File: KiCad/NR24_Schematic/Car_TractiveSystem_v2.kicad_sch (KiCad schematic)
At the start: 26 parts, among them J1 M_con, J2 F_con, J5 Dash TI Connection, J6 Deutsch, J7 Deutsch, J8 CAN Connector, K1 Line Contactor, K2 Key Switch Relay, M1 Zero_7R_Motor, SW1 TI power switch, SW2 Shifter Switch, SW3 100V E-stop (Right), SW4 100V E-stop (Left), SW5 Key Switch, SW6 12V E-stop, U1 Sevcon_Gen4_Size6, U2 Throttle

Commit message: v4
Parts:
- removed HVSS1: HV Safety Switch (behind driver), symbol CamachosSymbols:Safety Switch
- removed K1: Line Contactor, Relay_THT:Relay_1P1T_NO_10x24x18.8mm_Panasonic_ADW11xxxxW_THT, symbol Relay:ADW11
- removed LA1: TI power Light, symbol Device:Lamp
- removed LA2: FWD Light, symbol Device:Lamp
- removed LA3: Keyswitch Light, symbol Device:Lamp
- removed LA4: Fault Light, symbol Device:Lamp
- removed LA5: REV/N Light, symbol Device:Lamp
- removed SW1: TI power switch, symbol CamachosSymbols:SW_SPST
- removed SW2: Shifter Switch, symbol CamachosSymbols:SW_SPDT_MSM
- removed SW5: Key Switch, symbol CamachosSymbols:SW_SPST
- removed SW6: 12V E-stop, symbol Switch:SW_Push_Open
- added LA10: Keyswitch Light, symbol Device:Lamp
- added LA11: Fault Light, symbol Device:Lamp
- added LA7: TI power Light, symbol Device:Lamp
- added LA8: FWD Light, symbol Device:Lamp
- added LA9: REV/N Light, symbol Device:Lamp
- added SW10: Key Switch, symbol CamachosSymbols:SW_SPST
- added SW11: 12V E-stop, symbol Switch:SW_Push_Open
- added SW7: TI power switch, symbol CamachosSymbols:SW_SPST
- added SW9: Shifter Switch, symbol CamachosSymbols:SW_SPDT_MSM
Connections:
- net 12V+ to TI: now also LA7.2 (+), SW7.2 (B)
- net Dash +12V: now also SW11.2 (B), SW7.1 (A)
- net F_Light(+): now also LA8.2 (+)
- net F_Light(-): now also LA8.1 (-)
- net GND to TI: now also LA10.1 (-), LA7.1 (-)
- net N_Light(+): now also LA9.2 (+)
- net N_Light(-): now also LA9.1 (-)
- net Rocker_1: now also SW9.1
- net Rocker_2: now also SW9.2
- net Rocker_3: now also SW9.3
- net TI Fault Light(+): now also LA11.2 (+)
- net TI Fault Light(-): now also LA11.1 (-)
- net HV_Switch_Box/HV+: now reaches F1.2, U1. (M3)
- net at K2.1: now also LA10.2 (+), SW10.2 (B)
- new net: SW10.1 (A), SW11.1 (A)
- no-connect marks 10 -> 8
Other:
- added sheet Dash (Dash.kicad_sch)
- added sheet HV_Switch_Box (HV_Switch_Box.kicad_sch)
- sheet AMS Battery ports: added AIR, CAN_GND, CAN_High, CAN_Low, Charge Sig, HV +, HV -, TI Board; removed none
- sheet IMD ports: added AIR_In, AIR_Out, Dash_Error +, Dash_Error -, GND, HV_High, HV_Low, LV_High; removed none
- note removed: "ADD HV ACTIVE LIGHT HERE ^"
- note removed: "High Voltage Switch Box"

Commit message: B-? where are stops connected to
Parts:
- removed LA10: Keyswitch Light, symbol Device:Lamp
- removed LA11: Fault Light, symbol Device:Lamp
- removed LA6: IMD Safety Light, symbol Device:Lamp
- removed LA7: TI power Light, symbol Device:Lamp
- removed LA8: FWD Light, symbol Device:Lamp
- removed LA9: REV/N Light, symbol Device:Lamp
- removed SW10: Key Switch, symbol CamachosSymbols:SW_SPST
- removed SW11: 12V E-stop, symbol Switch:SW_Push_Open
- removed SW7: TI power switch, symbol CamachosSymbols:SW_SPST
- removed SW9: Shifter Switch, symbol CamachosSymbols:SW_SPDT_MSM
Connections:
- net GND to TI: no longer BTaux1.2 (-), J1.5 (Pin_5), K2.2, U1. (M3)
- net Dash/Key_SW +: now reaches K2.1
- net Dash +12V renamed Dash/12V Power
- new net B-: BTaux1.2 (-), J1.5 (Pin_5), K2.2, U1. (M3)
- no-connect marks 8 -> 6
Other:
- sheet Dash ports: added 12V Power, CAN_Data, Data_to_TI, GND, IMD Light, Key_SW +; removed none
- note removed: "Dash"
- note removed: "Dash CAN"
- note removed: "Display Screen"
- note removed: "|\--/| | o_o | \_ ^_/"
- moved on the sheet: BTaux1

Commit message: Please finish connection and AIR coils
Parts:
- removed J6, J7: Deutsch, symbol Connector_Generic:Conn_01x06
- added 3A: Fuse, symbol Device:Fuse
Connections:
- net CAN_High_fromSevcon: no longer U1.16 (Can_High)
- net CAN_Low_fromSevcon: no longer U1.27 (CAN_Low)
- net CAN_PWR_fromSevcon: no longer U1.28 (CAN_Power)
- net Dash/12V Power: now also 3A.1; no longer BTaux1.1 (+)
- net at U2.1 (pot_high_(red)): now also U1.34 (Pot1_PwrSupply+)
- net at U2.2 (pot_low_(blk)), U2.4 (sw_o/p_(yl)): now also U1. (M3)
- net at U2.3 (pot_wiper_(grn)): now also U1.22 (Pot1_WiperIn)
- net at U2.5 (sw_i/p_(blu)): now also U1.19 (Digital_FS1)
- new net: 3A.2, BTaux1.1 (+)
- no-connect marks 6 -> 2
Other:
- note removed: "Harness 1: Sevcon to Footwell"
- note removed: "Harness 4: CAN - Sevcon to TI Board"
- note removed: "Harness 5: Dash to Key Switch Relay"

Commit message: Please Finish Dash
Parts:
- removed J5: Dash TI Connection, symbol Connector_Generic:Conn_02x06_Counter_Clockwise
- removed J8: CAN Connector, symbol Connector_Generic:Conn_02x06_Counter_Clockwise
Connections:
- net Dash/12V Power is gone; now on net B-: 3A.1
- no-connect marks 2 -> 0
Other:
- note removed: "TI Board Box"
- note removed: "throttle_en and system_on connected to 5V off of the TI board (~20mA)"

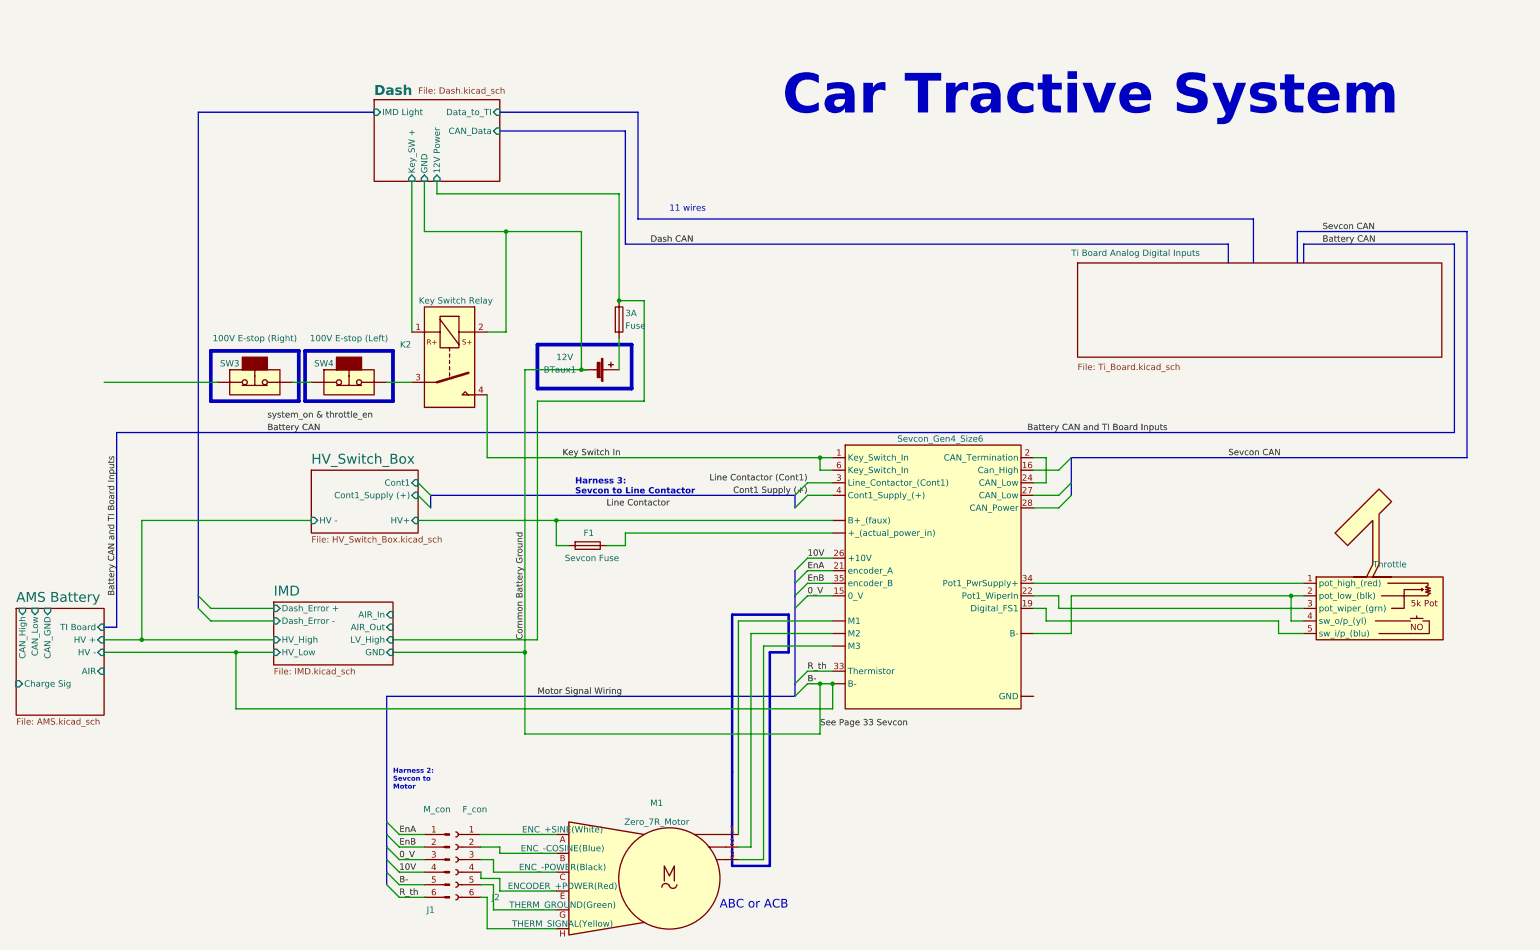
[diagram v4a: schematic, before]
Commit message: Almost there
Finish the key switch terminal, and the TI board schematic.
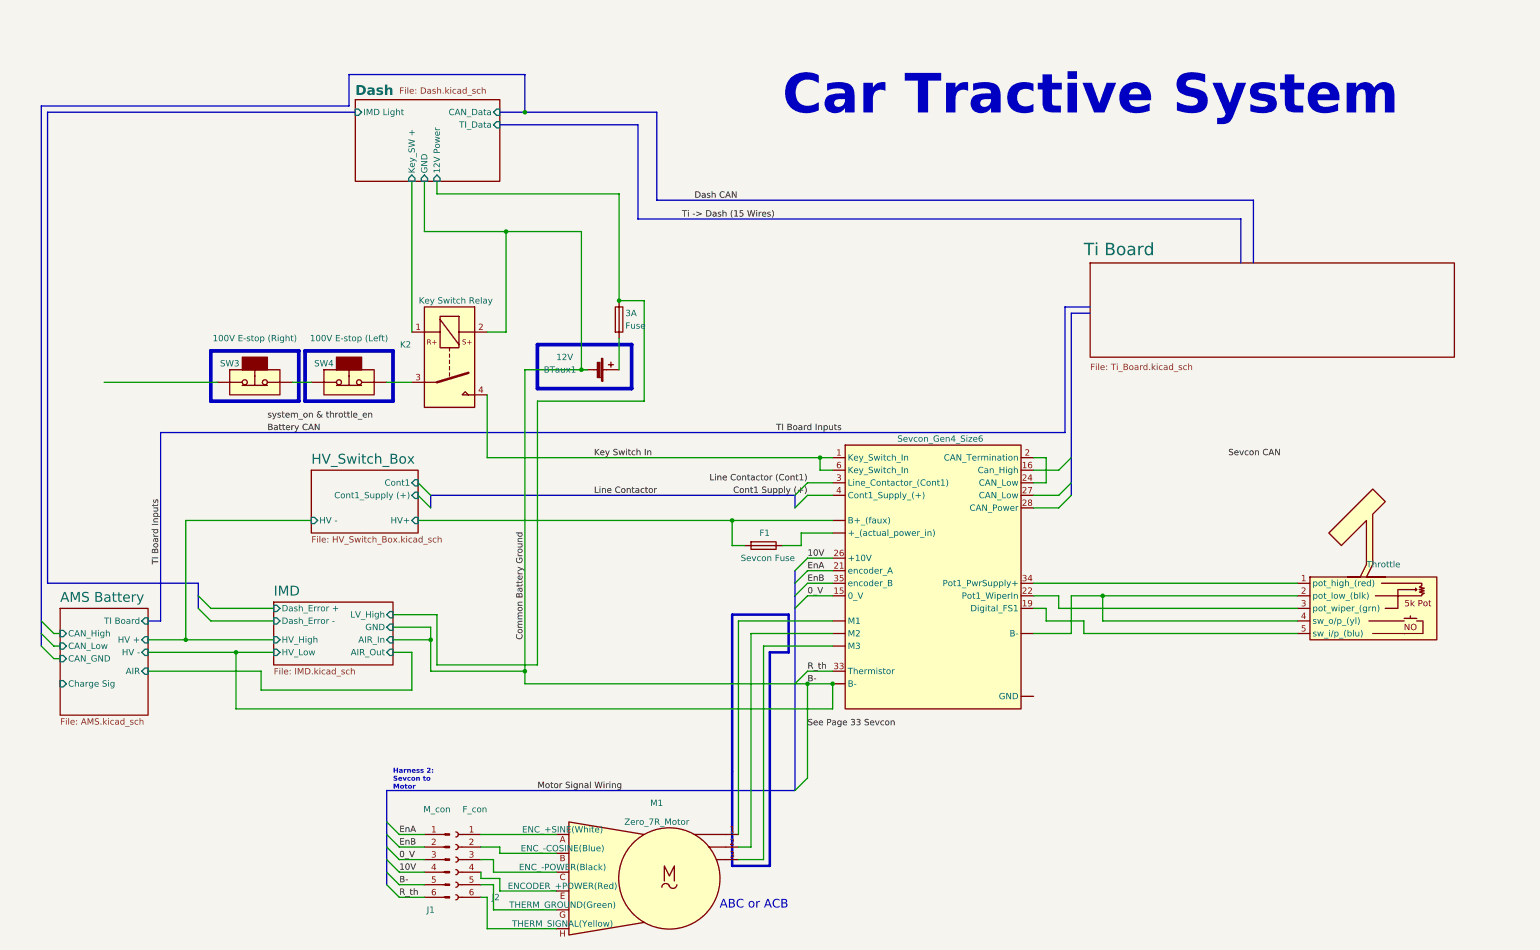
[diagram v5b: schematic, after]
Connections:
- net B-: no longer 3A.1
- new net Dash/12V Power: 3A.1
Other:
- sheet Ti Board Analog Digital Inputs renamed Ti Board
- sheet Dash ports: added TI_Data; removed Data_to_TI
- note removed: "11 wires"
- note removed: "Harness 3: Sevcon to Line Contactor"
- moved on the sheet: F1
